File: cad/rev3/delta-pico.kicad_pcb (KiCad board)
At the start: 2 copper layers, 77.7 x 159.8 mm, 73 parts, among them J1 Conn_01x02, J2 Conn_01x14, J3 Conn_01x04, J4 Conn_01x04, SW1 SW_SPDT, SW10 SW_Push, SW11 SW_Push, SW12 SW_Push, SW13 SW_Push, SW14 SW_Push, SW15 SW_Push, SW16 SW_Push, SW17 SW_Push, SW18 SW_Push, SW19 SW_Push, SW2 SW_Push, SW20 SW_Push, SW21 SW_Push, SW22 SW_Push, SW23 SW_Push, SW24 SW_Push, SW25 SW_Push, SW26 SW_Push, SW27 SW_Push, SW28 SW_Push, SW29 SW_Push, SW3 SW_Push, SW30 SW_Push, SW31 SW_Push, SW4 SW_Push, SW5 SW_Push, SW6 SW_Push, SW7 SW_Push, SW8 SW_Push, SW9 SW_Push, U1 PCF8574A, U2 PCF8574A, U3 Pico, U4 24LC16

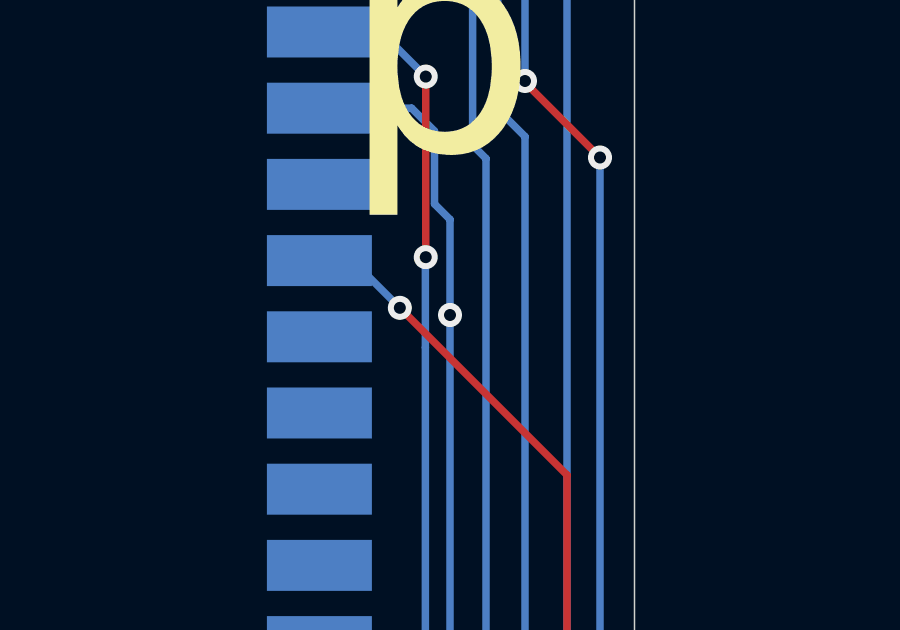
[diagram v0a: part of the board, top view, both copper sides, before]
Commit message: Remove pointless via
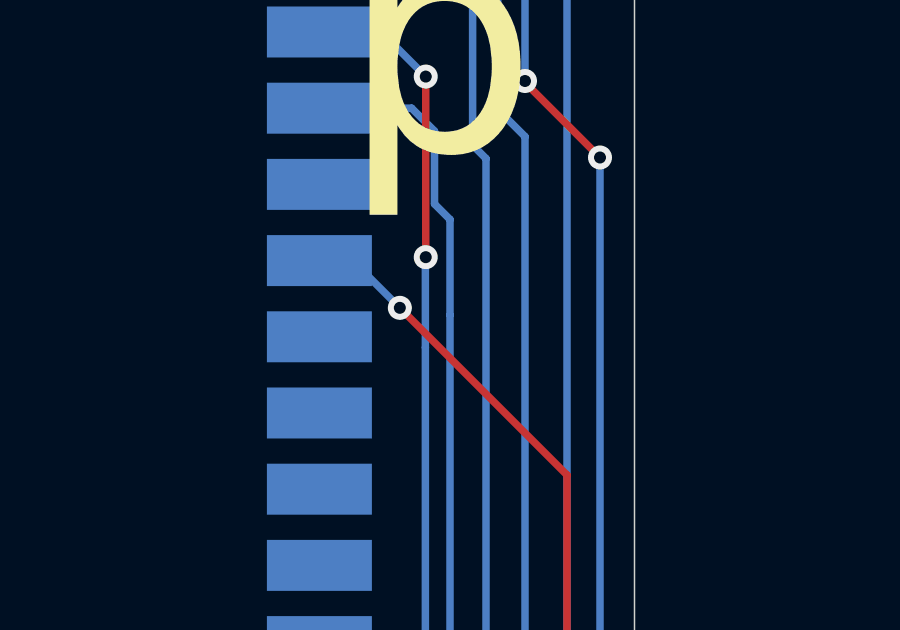
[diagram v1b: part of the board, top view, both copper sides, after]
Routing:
- net DC: vias 1 -> 0
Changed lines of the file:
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@@
   (segment (start 106.25 82.75) (end 106.25 46.5346) (width 0.25) (layer "B.Cu") (net 47))
   (segment (start 105.8037 40.9956) (end 104.5845 39.7764) (width 0.25) (layer "B.Cu") (net 47))
-  (via (at 105.05 51.75) (size 0.8) (drill 0.4) (layers "F.Cu" "B.Cu") (net 48))
   (segment (start 105.05 51.75) (end 105.05 48.564798) (width 0.25) (layer "B.Cu") (net 48))
   (segment (start 105.05 82.05) (end 105.05 51.75) (width 0.25) (layer "B.Cu") (net 48))

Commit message: Add a 6-pin "debug" port, in place of the expansion socket
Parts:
- removed the REF** at (36.7, 87.1)
- J3: value Conn_01x04 -> Conn_01x06; footprint Connector_PinHeader_2.54mm:PinHeader_1x04_P2.54mm_Vertical -> Connector_PinHeader_2.54mm:PinHeader_2x03_P2.54mm_Vertical
- moved J3 43.6 mm to (38.3, 104.8), turned to 0 degrees
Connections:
- J3 pad 1: SDA -> 3V3
- J3 pad 2: SCL -> GND
- J3 pad 3: GND -> SCL
- J3 pad 4: 3V3 -> SDA
- U3 pad 41: unconnected-(U3-Pad41) -> SWCLK
- U3 pad 43: unconnected-(U3-Pad43) -> SWDIO
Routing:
- net SWCLK: track 0.00 -> 71.6 mm, vias 0 -> 2
- net SWDIO: track 0.00 -> 63.3 mm
- net SCL: track 152.4 -> 167.1 mm, vias 4 -> 6
- net SDA: track 145.1 -> 155.0 mm
- net GND: track 246.2 -> 248.0 mm
- net 3V3: track 169.8 -> 171.1 mm, vias 7 -> 8
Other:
- board text added: "SWC"
- board text added: "SWD"

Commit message: Connect PCF8574 interrupt pins to GPIO 16/17
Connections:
- U1 pad 13: unconnected-(U1-Pad13) -> COLINT
- U2 pad 13: unconnected-(U2-Pad13) -> ROWINT
- U3 pad 21: unconnected-(U3-Pad21) -> COLINT
- U3 pad 22: unconnected-(U3-Pad22) -> ROWINT
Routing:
- net ROWINT: track 0.00 -> 63.5 mm, vias 0 -> 2
- net COLINT: track 0.00 -> 59.3 mm, vias 0 -> 2

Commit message: Break out some bonus GPIO and VIN
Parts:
- added J5: Conn_01x03, Connector_PinHeader_2.54mm:PinHeader_1x03_P2.54mm_Vertical, F.Cu at (57.5, 30.2)
- J3: value Conn_01x06 -> Conn_01x08; footprint Connector_PinHeader_2.54mm:PinHeader_2x03_P2.54mm_Vertical -> Connector_PinHeader_2.54mm:PinHeader_2x04_P2.54mm_Vertical
- moved J3 2.52 mm to (38.1, 102.3)
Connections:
- net Net-(J1-Pad1) renamed RAWVIN
- J3 pad 1: 3V3 -> GP19
- J3 pad 2: GND -> GP18
- J3 pad 3: SCL -> 3V3
- J3 pad 4: SDA -> GND
- J3 pad 5: SWCLK -> SCL
- J3 pad 6: SWDIO -> SDA
- U3 pad 24: unconnected-(U3-Pad24) -> GP18
- U3 pad 25: unconnected-(U3-Pad25) -> GP19
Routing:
- net GP19: track 0.00 -> 58.3 mm
- net GP18: track 0.00 -> 54.7 mm
- net RAWVIN: track 8.00 -> 31.6 mm, vias 0 -> 3
- net GND: track 248.0 -> 253.5 mm
- net VIN: track 48.3 -> 51.8 mm
- net 3V3: track 171.1 -> 173.2 mm
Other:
- board text added: "18"
- board text added: "19"
- board text added: "BYP. VIN"
- board text added: "SW. VIN"

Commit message: Add a 3D model for the display and use it
step.py uses FreeCAD to build SCAD into STEP
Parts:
- added REF**: ILI9341ModelOnly, DeltaPico:ILI9341ModelOnly, F.Cu at (48.1, 116.1)
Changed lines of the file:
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@@
+    )
+  )
+  (footprint "DeltaPico:ILI9341ModelOnly" (layer "F.Cu")
+    (at 48.07 116.12)
+    (attr smd)
+    (fp_text reference "REF**" (at 0 -0.5 unlocked) (layer "F.SilkS") hide
+      (effects (font (size 1 1) (thickness 0.15)))
+    )
+    (fp_text value "ILI9341ModelOnly" (at 0 1 unlocked) (layer "F.Fab")
+      (effects (font (size 1 1) (thickness 0.15)))
+    )
+    (fp_text user "${REFERENCE}" (at 0 2.5 unlocked) (layer "F.Fab") hide
+      (effects (font (size 1 1) (thickness 0.15)))
+    )
+    (model "${KIPRJMOD}/libraries/DeltaPico/DeltaPico.pretty/models/ili9341.step"
+      (offset (xyz 0 0 3))
+      (scale (xyz 1 1 1))
+      (rotate (xyz 0 0 0))
     )
   )
